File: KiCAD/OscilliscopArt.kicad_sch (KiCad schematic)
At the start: 5 parts, among them J1 Conn_01x09, J2 Conn_01x09, U1 MCP4902

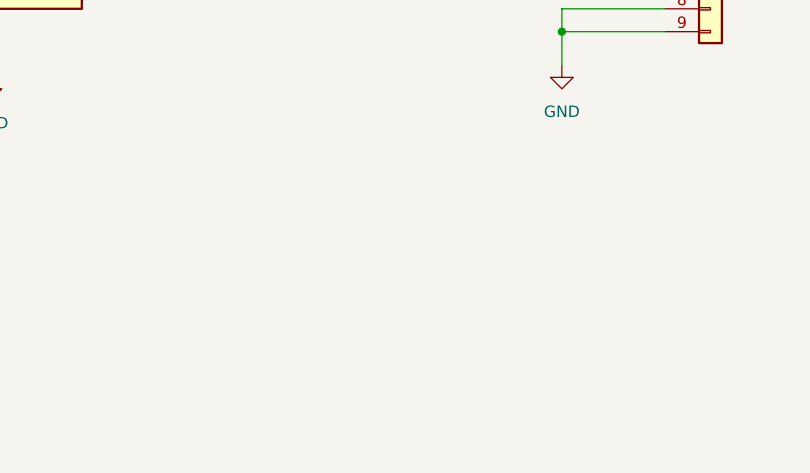
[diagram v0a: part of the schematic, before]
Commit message: Added SAO header
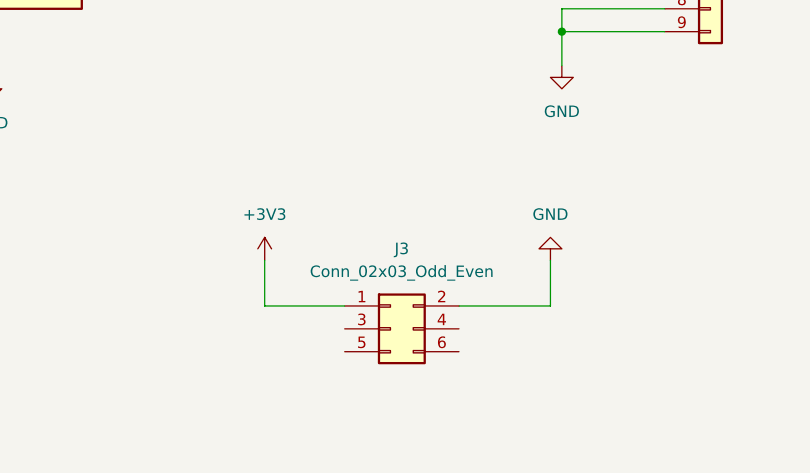
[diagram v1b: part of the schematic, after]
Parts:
- added J3: Conn_02x03_Odd_Even, Connector_PinHeader_2.54mm:PinHeader_2x03_P2.54mm_Vertical, symbol Connector_Generic:Conn_02x03_Odd_Even
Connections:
- net +3V3: now also J3.1 (Pin_1)
- net GND: now also J3.2 (Pin_2)
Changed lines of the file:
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@@
+	(wire
+		(pts
+			(xy 185.42 135.89) (xy 185.42 140.97)
+		)
+		(stroke
+			(width 0)
+			(type default)
+		)
+	)
 	(wire
 		(pts
@@
 	(wire
 		(pts
+			(xy 217.17 140.97) (xy 217.17 135.89)
+		)
+		(stroke
+			(width 0)
+			(type default)
+		)
+	)
+	(wire
+		(pts
 			(xy 215.9 97.79) (xy 229.87 97.79)
 		)
@@
 	(wire
 		(pts
+			(xy 185.42 140.97) (xy 194.31 140.97)
+		)
+		(stroke
+			(width 0)
+			(type default)
+		)
+	)
+	(wire
+		(pts
 			(xy 167.64 102.87) (xy 215.9 102.87)
 		)
@@
 		(pts
 			(xy 132.08 97.79) (xy 142.24 97.79)
+		)
+		(stroke
+			(width 0)
+			(type default)
+		)
+	)
+	(wire
+		(pts
+			(xy 207.01 140.97) (xy 217.17 140.97)
 		)
 		(stroke
@@
 			)
 			(justify left bottom)
+		)
+	)
+	(symbol
+		(lib_id "Connector_Generic:Conn_02x03_Odd_Even")
+		(at 199.39 143.51 0)
+		(unit 1)
+		(exclude_from_sim no)
+		(in_bom yes)
+		(on_board yes)
+		(dnp no)
+		(fields_autoplaced yes)
+		(property "Reference" "J3"
+			(at 200.66 134.62 0)
+			(effects
+				(font
+					(size 1.27 1.27)
+				)
+			)
+		)
+		(property "Value" "Conn_02x03_Odd_Even"
+			(at 200.66 137.16 0)
+			(effects
+				(font
+					(size 1.27 1.27)
+				)
+			)
+		)
+		(property "Footprint" "Connector_PinHeader_2.54mm:PinHeader_2x03_P2.54mm_Vertical"
+			(at 199.39 143.51 0)
+			(effects
+				(font
+					(size 1.27 1.27)
+				)
+				(hide yes)
+			)
+		)
+		(property "Datasheet" "~"
+			(at 199.39 143.51 0)
+			(effects
+				(font
+					(size 1.27 1.27)
+				)
+				(hide yes)
+			)
+		)
+		(property "Description" "Generic connector, double row, 02x03, odd/even pin numbering scheme (row 1 odd numbers, row 2 even numbers), script generated (kicad-library-utils/schlib/autogen/connector/)"
+			(at 199.39 143.51 0)
+			(effects
+				(font
+					(size 1.27 1.27)
+				)
+				(hide yes)
+			)
+		)
+		(pin "1"
+		)
+		(pin "5"
+		)
+		(pin "3"
+		)
+		(pin "4"
+		)
+		(pin "2"
+		)
+		(pin "6"
+		)
+		(instances
+			(project ""
+				(path "/a78b3458-4bc8-4087-8d51-399c24f5f89e"
+					(reference "J3")
+					(unit 1)
+				)
+			)
 		)
 	)
@@
 	)
 	(symbol
+		(lib_id "power:GND")
+		(at 217.17 135.89 180)
+		(unit 1)
+		(exclude_from_sim no)
+		(in_bom yes)
+		(on_board yes)
+		(dnp no)
+		(fields_autoplaced yes)
+		(property "Reference" "#PWR010"
+			(at 217.17 129.54 0)
+			(effects
+				(font
+					(size 1.27 1.27)
+				)
+				(hide yes)
+			)
+		)
+		(property "Value" "GND"
+			(at 217.17 130.81 0)
+			(effects
+				(font
+					(size 1.27 1.27)
+				)
+			)
+		)
+		(property "Footprint" ""
+			(at 217.17 135.89 0)
+			(effects
+				(font
+					(size 1.27 1.27)
+				)
+				(hide yes)
+			)
+		)
+		(property "Datasheet" ""
+			(at 217.17 135.89 0)
+			(effects
+				(font
+					(size 1.27 1.27)
+				)
+				(hide yes)
+			)
+		)
+		(property "Description" "Power symbol creates a global label with name \"GND\" , ground"
+			(at 217.17 135.89 0)
+			(effects
+				(font
+					(size 1.27 1.27)
+				)
+				(hide yes)
+			)
+		)
+		(pin "1"
+		)
+		(instances
+			(project "OscilliscopArt"
+				(path "/a78b3458-4bc8-4087-8d51-399c24f5f89e"
+					(reference "#PWR010")
+					(unit 1)
+				)
+			)
+		)
+	)
+	(symbol
 		(lib_id "power:+3V3")
 		(at 154.94 77.47 0)
@@
 					(unit 1)
 				)
+			)
+		)
+	)
+	(symbol
+		(lib_id "power:+3V3")
+		(at 185.42 135.89 0)
+		(unit 1)
+		(exclude_from_sim no)
+		(in_bom yes)
+		(on_board yes)
+		(dnp no)
+		(fields_autoplaced yes)
+		(property "Reference" "#PWR09"
+			(at 185.42 139.7 0)
+			(effects
+				(font
+					(size 1.27 1.27)
+				)
+				(hide yes)
+			)
+		)
+		(property "Value" "+3V3"
+			(at 185.42 130.81 0)
+			(effects
+				(font
+					(size 1.27 1.27)
+				)
+			)
+		)
+		(property "Footprint" ""
+			(at 185.42 135.89 0)
+			(effects
+				(font
+					(size 1.27 1.27)
+				)
+				(hide yes)
+			)
+		)
+		(property "Datasheet" ""
+			(at 185.42 135.89 0)
+			(effects
+				(font
+					(size 1.27 1.27)
+				)
+				(hide yes)
+			)
+		)
+		(property "Description" "Power symbol creates a global label with name \"+3V3\""
+			(at 185.42 135.89 0)
+			(effects
+				(font
+					(size 1.27 1.27)
+				)
+				(hide yes)
+			)
+		)
+		(pin "1"
+		)
+		(instances
+			(project "OscilliscopArt"
+				(path "/a78b3458-4bc8-4087-8d51-399c24f5f89e"
+					(reference "#PWR09")
+					(unit 1)
+				)
